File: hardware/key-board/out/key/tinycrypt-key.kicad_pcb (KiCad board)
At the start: 2 copper layers, 21 x 40 mm, 24 parts, among them J1 SM05B-SRSS-G-TB, SW1 TS-1187A-B-A-B, U1 ESP32-S3-MINI-1-N8, U2 AP2112K-3.3TRG1, U3 USBLC6-2SC6, U4 ATECC608B-SSHDA-T

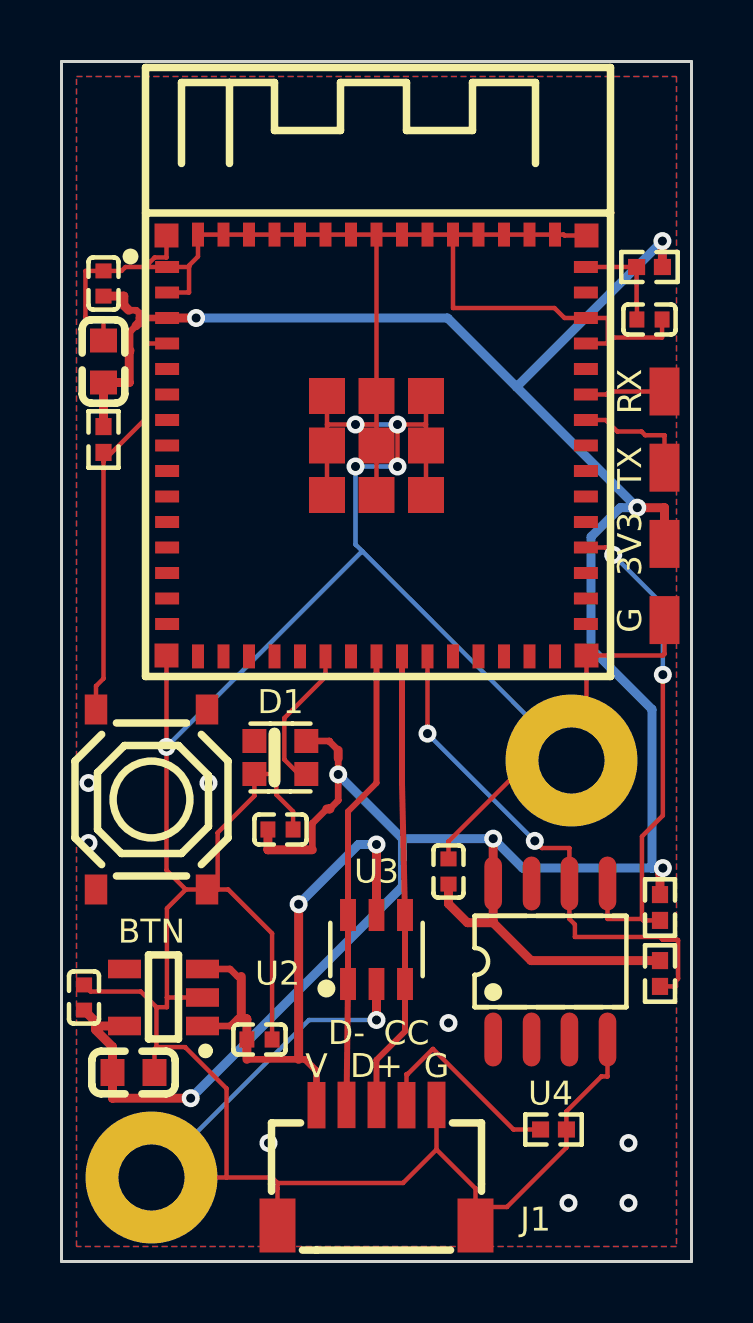
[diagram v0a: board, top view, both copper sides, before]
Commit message: build(hardware): key board outputs after the review fixes, DRC clean (CRYPT-16)
out/key from build.py --board key --route: 21 x 34.95 mm, DRC 0 errors,
0 unconnected, 0 warnings; BOM 14 lines (6 Extended), CPL, gerbers zip,
renders, pins.h.
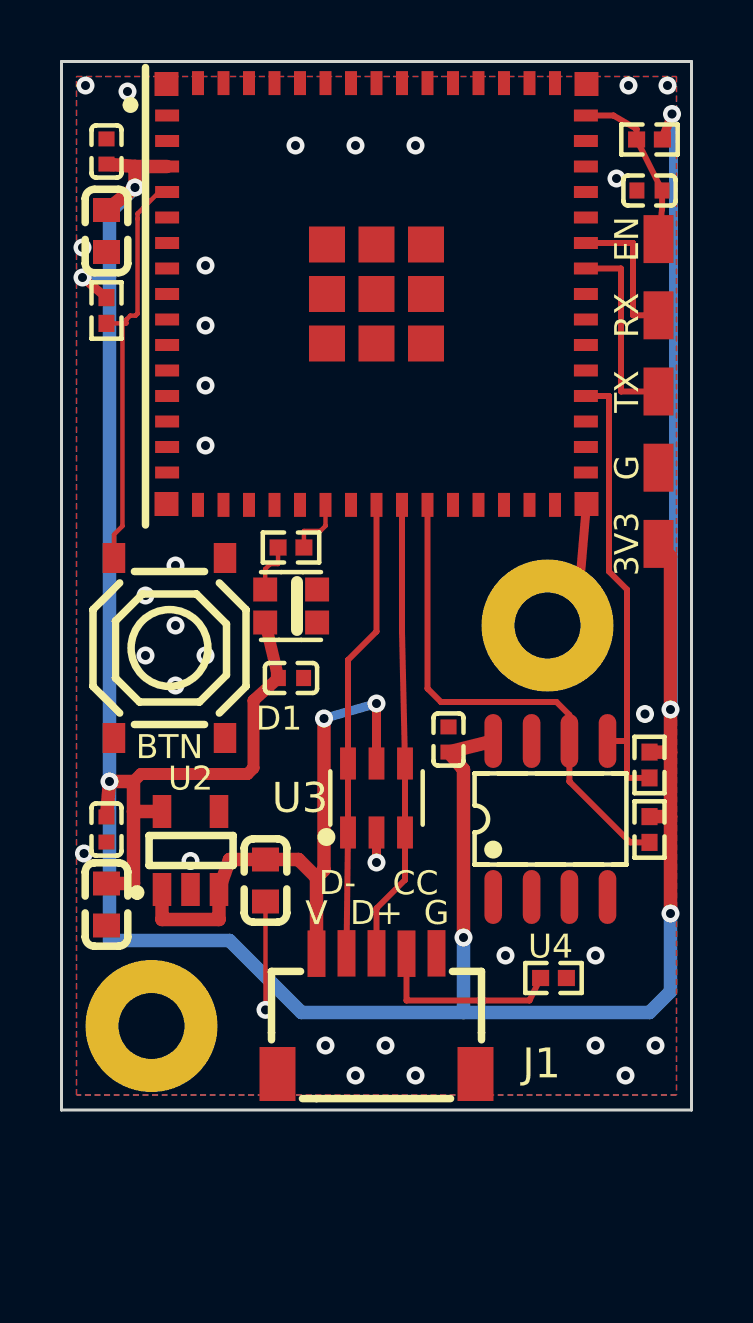
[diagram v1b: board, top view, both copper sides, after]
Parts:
- added R6: 330R, R0402, F.Cu at (7.65, 16.2)
- C1: value 1uF -> 10uF; footprint C0402 -> C0603
- TP1: footprint DebugPads_1x4_P2.54 -> DebugPads_1x5_P2.54
- moved C2 5.67 mm to (1.50, 28.1), turned to -90 degrees
- moved C3 5.65 mm to (1.50, 25.6), turned to -90 degrees
- moved C1 5.30 mm to (6.80, 27.3), turned to -90 degrees
- moved SW1 5.09 mm to (3.60, 19.6)
- moved C8 5.06 mm to (7.65, 20.6)
- moved D1 5.06 mm to (7.65, 18.1), turned to 180 degrees
- moved H2 5.05 mm to (3.00, 32.1)
- moved J1 5.05 mm to (10.5, 31.7)
- moved R1 5.05 mm to (16.4, 30.6)
- moved U1 5.05 mm to (10.5, 7.75)
- moved U3 5.05 mm to (10.5, 24.6)
- moved U2 4.98 mm to (4.30, 26.3), turned to 0 degrees
- moved R5 4.81 mm to (19.6, 25.6)
- moved R4 4.76 mm to (19.6, 23.4)
- moved U4 4.75 mm to (16.3, 25.2)
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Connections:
- TP1 pad 1: UART_RX -> EN
- TP1 pad 2: UART_TX -> UART_RX
- TP1 pad 3: +3V3 -> UART_TX
- U1 pad 21: LED_DIN -> LED_GPIO
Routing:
- net GND: track 166.7 -> 6.97 mm, vias 14 -> 33
- net +3V3: track 99.2 -> 115.7 mm
- net LED_DIN: track 4.94 -> 1.73 mm
- net UART_TX: track 3.91 -> 6.52 mm
- net EN: track 3.44 -> 5.69 mm
- net UART_RX: track 2.66 -> 4.83 mm
- net LED_GPIO: track 0.00 -> 2.04 mm
- net SDA: track 17.1 -> 15.1 mm, vias 2 -> 0
- net SCL: track 17.5 -> 16.9 mm, vias 2 -> 0
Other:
- board size 21 x 40 mm -> 21 x 35 mm
- board text added: "EN"
- board text added: "MODULE ANTENNA OVERHANGS THIS EDGE BY 5.05 mm: INTENTIONAL"
